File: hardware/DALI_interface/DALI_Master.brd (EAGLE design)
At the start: 49.5 x 28 mm, 25 parts, among them IC1 LM393D, Q1 BD135, Q2 BC817-25, Q3 BC817-25, X1 MKDSN1,5/2-5,08, X2 MKDSN1,5/2-5,08

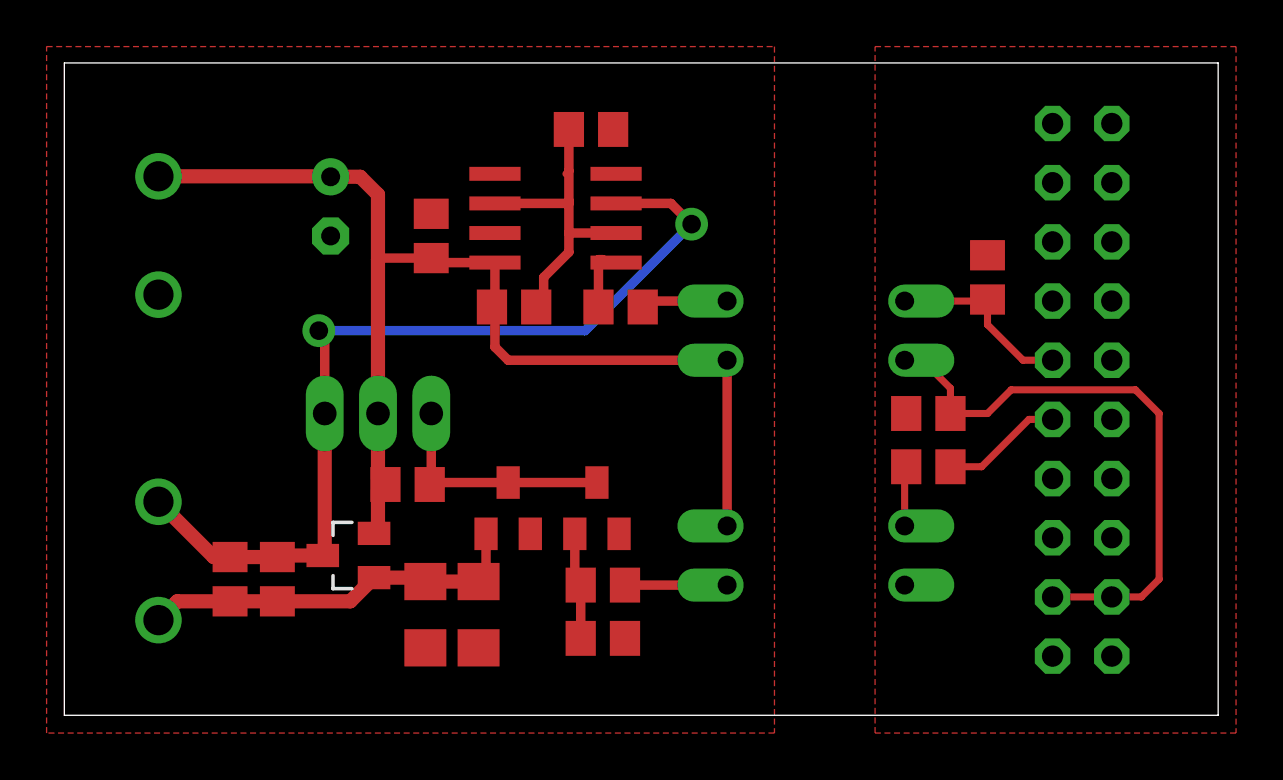
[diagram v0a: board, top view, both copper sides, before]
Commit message: added the missing resistor values and a reference to the site with the original idea
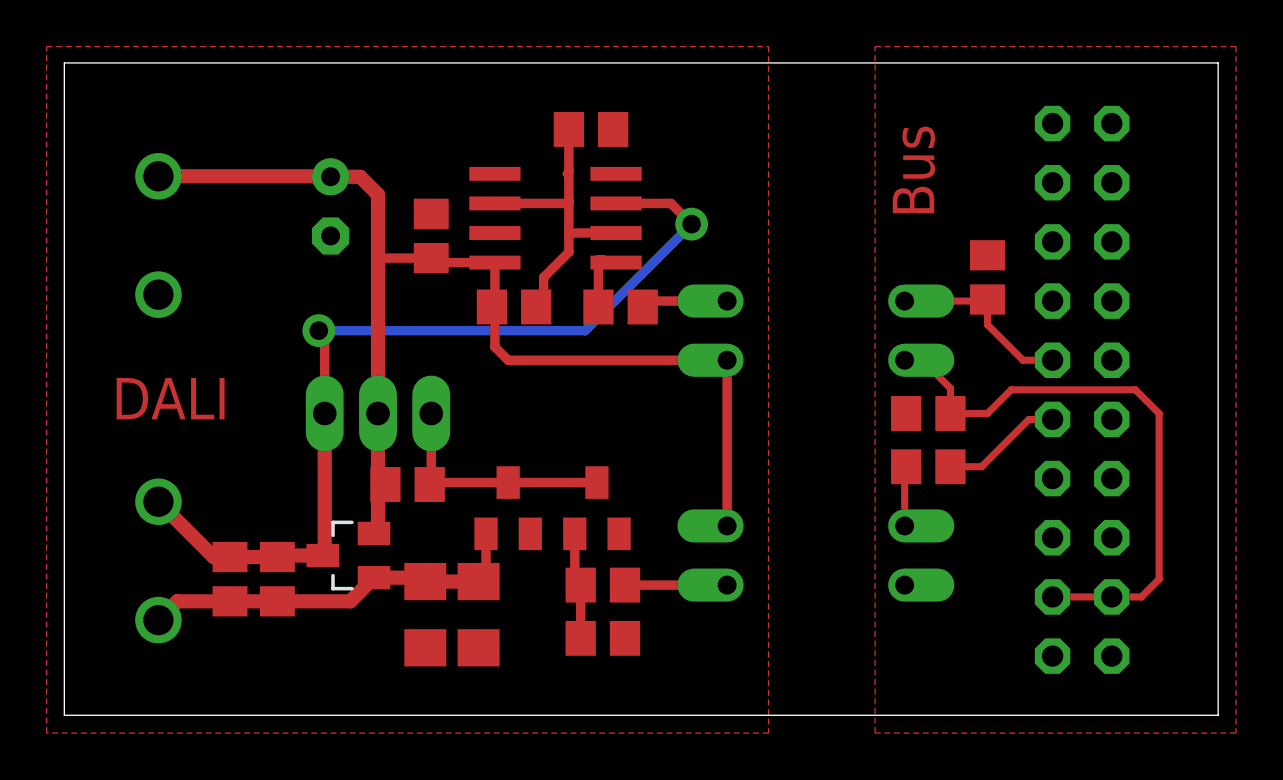
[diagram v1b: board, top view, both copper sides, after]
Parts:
- R10, R11: value (none) -> 1k
- R7: value (none) -> 470R
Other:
- board text added: "Bus"
- board text added: "DALI"
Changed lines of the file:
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@@
 <wire x1="49.524" y1="28" x2="0" y2="28" width="0" layer="20"/>
 <wire x1="0" y1="28" x2="0" y2="0" width="0" layer="20"/>
+<text x="2.032" y="12.7" size="1.778" layer="1" font="vector" ratio="14">DALI</text>
+<text x="37.338" y="21.336" size="1.778" layer="1" font="vector" ratio="14" rot="R90">Bus</text>
 </plain>
 <attributes>
@@
 <element name="R6" library="rcl" package="R0805" value="1k" x="23.114" y="5.588" smashed="yes"/>
 <element name="R5" library="rcl" package="R0805" value="1k" x="14.732" y="9.906" smashed="yes" rot="R180"/>
-<element name="R7" library="rcl" package="R0805" value="" x="37.084" y="10.668" smashed="yes">
-<attribute name="VALUE" x="36.449" y="8.128" size="1.27" layer="27"/>
-</element>
+<element name="R7" library="rcl" package="R0805" value="470R" x="37.084" y="10.668" smashed="yes"/>
 <element name="R8" library="rcl" package="R1206" value="5R6" x="17.78" y="4.318" smashed="yes" rot="R90"/>
 <element name="R9" library="rcl" package="R1206" value="5R6" x="15.494" y="4.318" smashed="yes" rot="R90"/>
 <element name="C3" library="rcl" package="C0805" value="220n" x="7.112" y="5.842" smashed="yes" rot="R90"/>
 <element name="D1" library="diode" package="SOT23" value="BAT54S" x="12.192" y="6.858" smashed="yes" rot="R90"/>
-<element name="R10" library="rcl" package="R0805" value="" x="9.144" y="5.842" smashed="yes" rot="R90">
-<attribute name="VALUE" x="11.684" y="5.207" size="1.27" layer="27" rot="R90"/>
-</element>
+<element name="R10" library="rcl" package="R0805" value="1k" x="9.144" y="5.842" smashed="yes" rot="R90"/>
 <element name="C4" library="rcl" package="E2,5-6" value="100u" x="11.43" y="21.844" smashed="yes" rot="MR270"/>
-<element name="R11" library="rcl" package="R0805" value="" x="39.624" y="18.796" smashed="yes" rot="R270">
-<attribute name="VALUE" x="37.084" y="19.431" size="1.27" layer="27" rot="R270"/>
-</element>
-<element name="OK3" library="optocoupler" package="DIL04" value="LTV816" x="32.258" y="16.51" rot="MR90">
+<element name="R11" library="rcl" package="R0805" value="1k" x="39.624" y="18.796" smashed="yes" rot="R270"/>
+<element name="OK3" library="optocoupler" package="DIL04" value="LTV816" x="32.258" y="16.51" smashed="yes" rot="MR90">
 <attribute name="OC_NEWARK" value="unknown" x="32.258" y="16.51" size="1.778" layer="28" rot="MR90" display="off"/>
 <attribute name="MPN" value="" x="32.258" y="16.51" size="1.778" layer="28" rot="MR90" display="off"/>
@@
 <attribute name="OC_FARNELL" value="unknown" x="32.258" y="16.51" size="1.778" layer="28" rot="MR90" display="off"/>
 </element>
-<element name="OK4" library="optocoupler" package="DIL04" value="LTV816" x="32.258" y="6.858" rot="MR270">
+<element name="OK4" library="optocoupler" package="DIL04" value="LTV816" x="32.258" y="6.858" smashed="yes" rot="MR270">
 <attribute name="OC_NEWARK" value="unknown" x="32.258" y="6.858" size="1.778" layer="28" rot="MR270" display="off"/>
 <attribute name="MPN" value="" x="32.258" y="6.858" size="1.778" layer="28" rot="MR270" display="off"/>
@@
 <polygon width="0.254" layer="1" isolate="0.3048">
 <vertex x="-0.762" y="28.702"/>
-<vertex x="30.48" y="28.702"/>
-<vertex x="30.48" y="-0.762"/>
+<vertex x="30.226" y="28.702"/>
+<vertex x="30.226" y="-0.762"/>
 <vertex x="-0.762" y="-0.762"/>
 </polygon>

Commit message: changed some resistor values
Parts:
- R10: value 1k -> 1k5
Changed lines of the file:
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@@
 <element name="C3" library="rcl" package="C0805" value="220n" x="7.112" y="5.842" smashed="yes" rot="R90"/>
 <element name="D1" library="diode" package="SOT23" value="BAT54S" x="12.192" y="6.858" smashed="yes" rot="R90"/>
-<element name="R10" library="rcl" package="R0805" value="1k" x="9.144" y="5.842" smashed="yes" rot="R90"/>
+<element name="R10" library="rcl" package="R0805" value="1k5" x="9.144" y="5.842" smashed="yes" rot="R90"/>
 <element name="C4" library="rcl" package="E2,5-6" value="100u" x="11.43" y="21.844" smashed="yes" rot="MR270"/>
 <element name="R11" library="rcl" package="R0805" value="1k" x="39.624" y="18.796" smashed="yes" rot="R270"/>

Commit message: change the value of the capacitor on the bus to be in spec
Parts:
- C3: value 220n -> 100n
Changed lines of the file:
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@@
 <element name="R8" library="rcl" package="R1206" value="5R6" x="17.78" y="4.318" smashed="yes" rot="R90"/>
 <element name="R9" library="rcl" package="R1206" value="5R6" x="15.494" y="4.318" smashed="yes" rot="R90"/>
-<element name="C3" library="rcl" package="C0805" value="220n" x="7.112" y="5.842" smashed="yes" rot="R90"/>
+<element name="C3" library="rcl" package="C0805" value="100n" x="7.112" y="5.842" smashed="yes" rot="R90"/>
 <element name="D1" library="diode" package="SOT23" value="BAT54S" x="12.192" y="6.858" smashed="yes" rot="R90"/>
 <element name="R10" library="rcl" package="R0805" value="1k5" x="9.144" y="5.842" smashed="yes" rot="R90"/>
